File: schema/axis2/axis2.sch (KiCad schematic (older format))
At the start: 15 parts, among them J1 JA, J2 JB, J3 5VPower, J4 12VPower, J5 Power Motor 1, J6 Power Motor 2, J7 M1, J8 M2, J9 RC-PPM, U1 gy-9250, U2 L7805, U3 axis2-frame

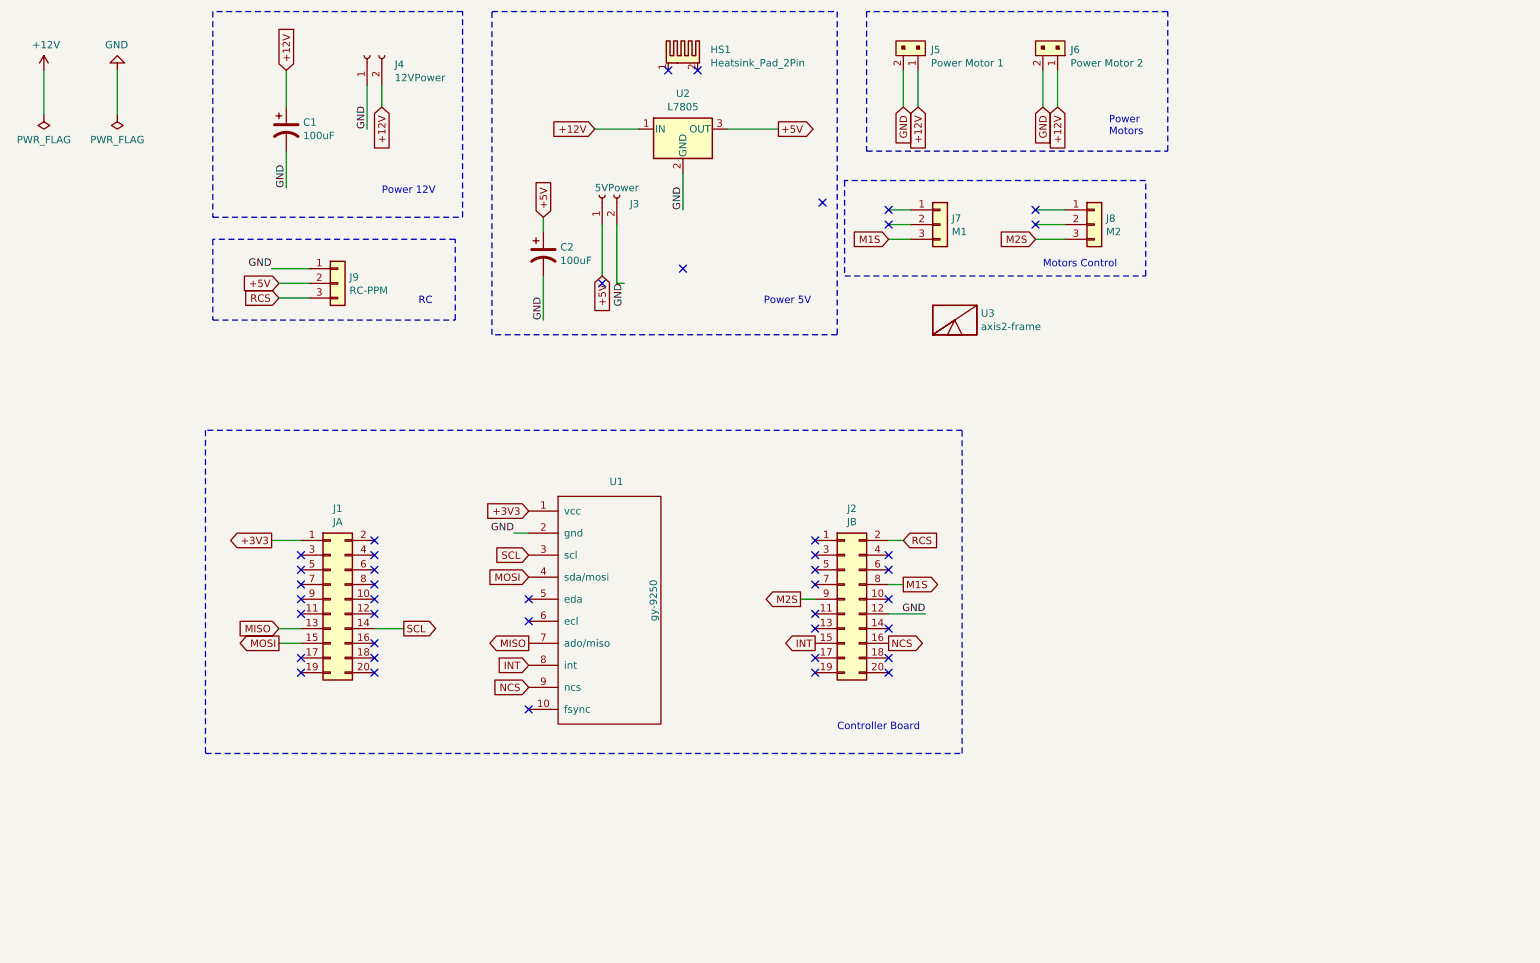
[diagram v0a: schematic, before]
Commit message: Corretto scheda e testato relay per switch on/off motori. Implementato ciclo di switch on/off motori
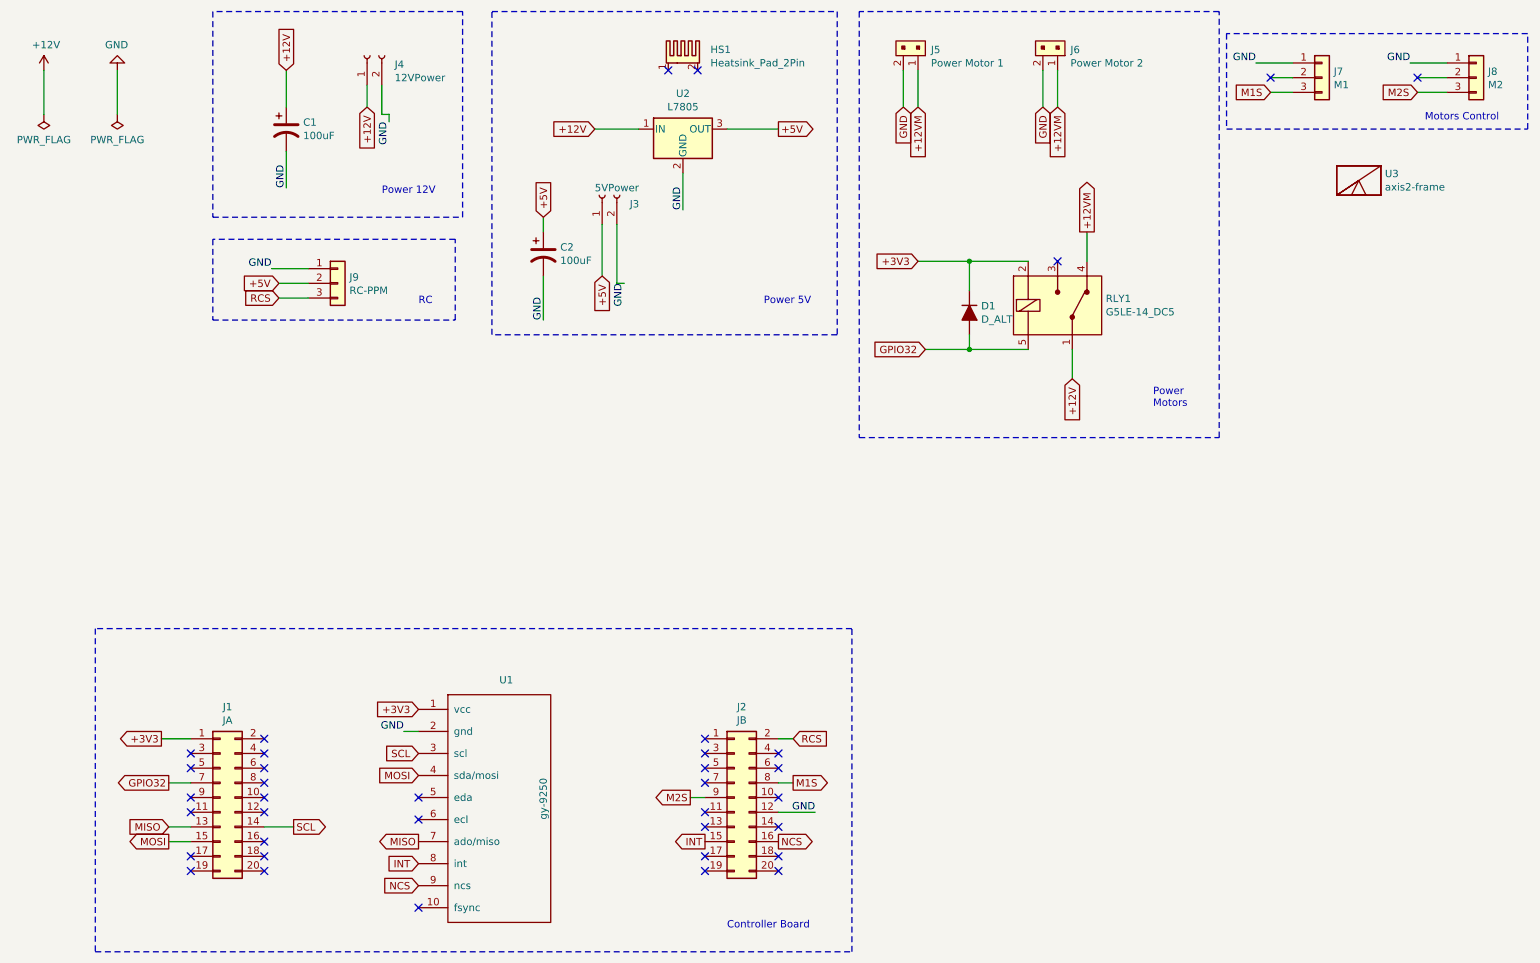
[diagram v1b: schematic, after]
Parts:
- added D1: D_ALT, Diode_THT:D_DO-34_SOD68_P7.62mm_Horizontal, symbol Device:D_ALT
- added RLY1: G5LE-14_DC5, Relay_THT:Relay_SPDT_Omron-G5LE-1, symbol dk_Power-Relays-Over-2-Amps:G5LE-14_DC5
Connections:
- net +12V: now also J4.1 (Pin_1), RLY1.1 (COM); no longer J4.2 (Pin_2), J5.1, J6.1
- net +3V3: now also D1.1 (K), RLY1.2 (COIL)
- net GND: now also J4.2 (Pin_2), J7.1 (Pin_1), J8.1 (Pin_1); no longer J4.1 (Pin_1)
- net GPIO32: now reaches J1.7 (Pin_7)
- net GPIO32: now also D1.2 (A), RLY1.5 (COIL)
- new net +12VM: J5.1, J6.1, RLY1.4 (NC)
- no-connect marks 42 -> 37
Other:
- moved on the sheet: J1, J2, J7, J8, U1, U3

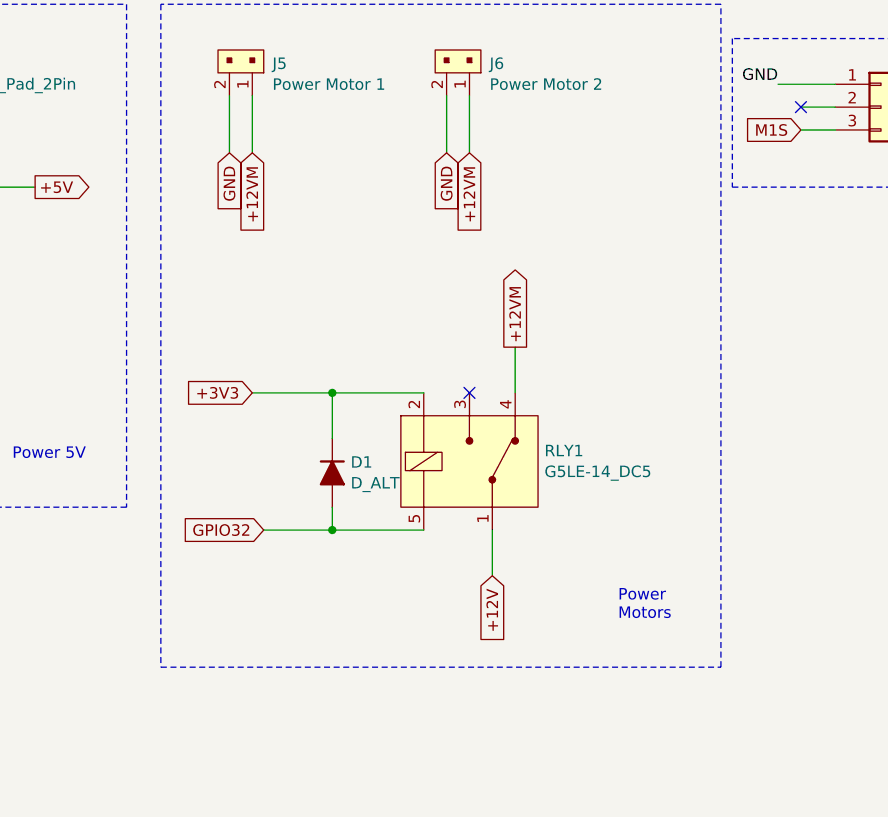
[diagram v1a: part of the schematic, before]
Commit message: Modificato scheda aggiungendo BC547.
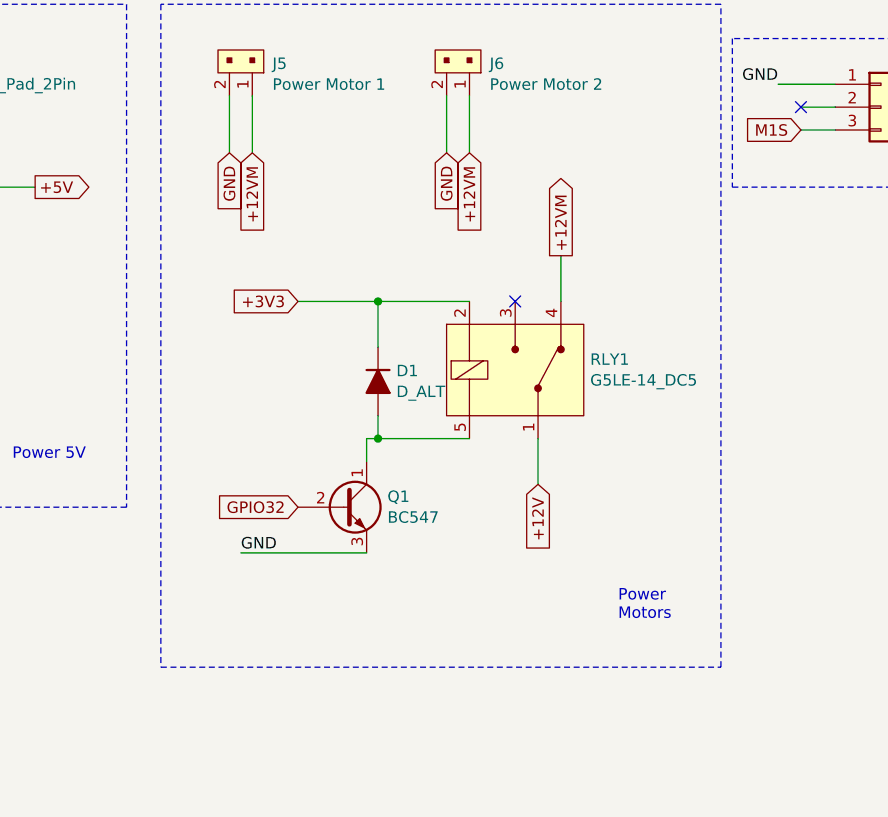
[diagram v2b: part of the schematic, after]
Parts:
- added Q1: BC547, Package_TO_SOT_THT:TO-92, symbol Transistor_BJT:BC547
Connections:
- net GND: now also Q1.3 (E)
- net GPIO32: now also Q1.2 (B); no longer D1.2 (A), RLY1.5 (COIL)
- new net: D1.2 (A), Q1.1 (C), RLY1.5 (COIL)
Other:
- moved on the sheet: D1, RLY1
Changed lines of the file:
@@
 L dk_Power-Relays-Over-2-Amps:G5LE-14_DC5 RLY1
 U 1 1 608096DF
-P 7950 2700
-F 0 "RLY1" H 8278 2746 50  0000 L CNN
-F 1 "G5LE-14_DC5" H 8278 2655 50  0000 L CNN
-F 2 "Relay_THT:Relay_SPDT_Omron-G5LE-1" H 8150 2900 50  0001 L CNN
-F 3 "https://omronfs.omron.com/en_US/ecb/products/pdf/en-g5le.pdf" H 8150 3000 60  0001 L CNN
-F 4 "Z1011-ND" H 8150 3100 60  0001 L CNN "Digi-Key_PN"
-F 5 "G5LE-14 DC5" H 8150 3200 60  0001 L CNN "MPN"
-F 6 "Relays" H 8150 3300 60  0001 L CNN "Category"
-F 7 "Power Relays, Over 2 Amps" H 8150 3400 60  0001 L CNN "Family"
-F 8 "https://omronfs.omron.com/en_US/ecb/products/pdf/en-g5le.pdf" H 8150 3500 60  0001 L CNN "DK_Datasheet_Link"
-F 9 "/product-detail/en/omron-electronics-inc-emc-div/G5LE-14-DC5/Z1011-ND/280371" H 8150 3600 60  0001 L CNN "DK_Detail_Page"
-F 10 "RELAY GEN PURPOSE SPDT 10A 5V" H 8150 3700 60  0001 L CNN "Description"
-F 11 "Omron Electronics Inc-EMC Div" H 8150 3800 60  0001 L CNN "Manufacturer"
-F 12 "Active" H 8150 3900 60  0001 L CNN "Status"
-	1    7950 2700
+P 8150 2300
+F 0 "RLY1" H 8478 2346 50  0000 L CNN
+F 1 "G5LE-14_DC5" H 8478 2255 50  0000 L CNN
+F 2 "Relay_THT:Relay_SPDT_Omron-G5LE-1" H 8350 2500 50  0001 L CNN
+F 3 "https://omronfs.omron.com/en_US/ecb/products/pdf/en-g5le.pdf" H 8350 2600 60  0001 L CNN
+F 4 "Z1011-ND" H 8350 2700 60  0001 L CNN "Digi-Key_PN"
+F 5 "G5LE-14 DC5" H 8350 2800 60  0001 L CNN "MPN"
+F 6 "Relays" H 8350 2900 60  0001 L CNN "Category"
+F 7 "Power Relays, Over 2 Amps" H 8350 3000 60  0001 L CNN "Family"
+F 8 "https://omronfs.omron.com/en_US/ecb/products/pdf/en-g5le.pdf" H 8350 3100 60  0001 L CNN "DK_Datasheet_Link"
+F 9 "/product-detail/en/omron-electronics-inc-emc-div/G5LE-14-DC5/Z1011-ND/280371" H 8350 3200 60  0001 L CNN "DK_Detail_Page"
+F 10 "RELAY GEN PURPOSE SPDT 10A 5V" H 8350 3300 60  0001 L CNN "Description"
+F 11 "Omron Electronics Inc-EMC Div" H 8350 3400 60  0001 L CNN "Manufacturer"
+F 12 "Active" H 8350 3500 60  0001 L CNN "Status"
+	1    8150 2300
 	1    0    0    -1
 $EndComp
-Text GLabel 7050 3000 0    50   Input ~ 0
+Text GLabel 7200 2900 0    50   Input ~ 0
 GPIO32
-Text GLabel 8050 3200 3    50   Input ~ 0
+Text GLabel 8250 2800 3    50   Input ~ 0
 +12V
 Wire Wire Line
-	8050 3200 8050 3000
-Text GLabel 8150 2200 1    50   Output ~ 0
+	8250 2800 8250 2600
+Text GLabel 8350 1800 1    50   Output ~ 0
 +12VM
 Wire Wire Line
-	8150 2400 8150 2200
-NoConn ~ 7950 2400
+	8350 2000 8350 1800
+NoConn ~ 8150 2000
 Text GLabel 1900 5950 0    50   Output ~ 0
 GPIO32
@@
 L Device:D_ALT D1
 U 1 1 60836FCC
-P 7350 2750
-F 0 "D1" V 7304 2830 50  0000 L CNN
-F 1 "D_ALT" V 7395 2830 50  0000 L CNN
-F 2 "Diode_THT:D_DO-34_SOD68_P7.62mm_Horizontal" H 7350 2750 50  0001 C CNN
-F 3 "~" H 7350 2750 50  0001 C CNN
-	1    7350 2750
+P 7550 2350
+F 0 "D1" V 7504 2430 50  0000 L CNN
+F 1 "D_ALT" V 7595 2430 50  0000 L CNN
+F 2 "Diode_THT:D_DO-34_SOD68_P7.62mm_Horizontal" H 7550 2350 50  0001 C CNN
+F 3 "~" H 7550 2350 50  0001 C CNN
+	1    7550 2350
 	0    1    1    0
 $EndComp
 Wire Wire Line
-	7350 2600 7350 2400
-Connection ~ 7350 2400
+	7550 2200 7550 2000
+Connection ~ 7550 2000
 Wire Wire Line
-	7350 2400 7750 2400
+	7550 2000 7950 2000
 Wire Wire Line
-	7350 2900 7350 3000
-Connection ~ 7350 3000
+	7550 2500 7550 2600
+Connection ~ 7550 2600
 Wire Wire Line
-	7350 3000 7750 3000
-Text GLabel 7000 2400 0    50   Input ~ 0
+	7550 2600 7950 2600
+Text GLabel 7200 2000 0    50   Input ~ 0
 +3V3
 Wire Wire Line
-	7000 2400 7350 2400
-Wire Wire Line
-	7050 3000 7350 3000
+	7200 2000 7550 2000
 Wire Notes Line
 	6600 3600 9050 3600
@@
 Wire Notes Line
 	6600 700  6600 3600
+$Comp
+L Transistor_BJT:BC547 Q1
+U 1 1 60841F0D
+P 7400 2900
+F 0 "Q1" H 7591 2946 50  0000 L CNN
+F 1 "BC547" H 7591 2855 50  0000 L CNN
+F 2 "Package_TO_SOT_THT:TO-92" H 7600 2825 50  0001 L CIN
+F 3 "https://www.onsemi.com/pub/Collateral/BC550-D.pdf" H 7400 2900 50  0001 L CNN
+	1    7400 2900
+	1    0    0    -1
+$EndComp
+Text Label 6950 3100 0    50   ~ 0
+GND
+Wire Wire Line
+	7500 2700 7500 2600
+Wire Wire Line
+	7500 2600 7550 2600
+Wire Wire Line
+	7500 3100 6950 3100
 $EndSCHEMATC
